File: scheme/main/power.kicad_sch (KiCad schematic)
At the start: 3 parts, among them U15 SCWN06B-15, U16 K7809-1000R3, U17 K7803-1000R3

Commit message: power scheme
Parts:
- added C61, C63: 22uF, Capacitor_SMD:C_Elec_4x5.8, symbol Device:C_Polarized
- added C62, C64, C66, C68, C70, C72, C76, C78, C80, C82: 220nF, Capacitor_SMD:C_0805_2012Metric, symbol Device:C
- added C65, C67, C69, C71, C75, C77, C81: 47uF, Capacitor_SMD:C_Elec_5x5.8, symbol Device:C_Polarized
- added C73, C74: 33nF, Capacitor_SMD:C_0805_2012Metric, symbol Device:C
- added C79: 4.7uF, Capacitor_SMD:C_0805_2012Metric, symbol Device:C
- added L1: 160uH, Inductor_SMD:L_0805_2012Metric, symbol Device:L
- added NT1: NetTie_2, symbol Device:NetTie_2
- added U18: LD1117S50TR_SOT223, Package_TO_SOT_SMD:SOT-223-3_TabPin2, symbol Regulator_Linear:LD1117S50TR_SOT223
- added U19: IFX1117MEV33HTMA1, Package_TO_SOT_SMD:SOT-223-3_TabPin2, symbol Regulator_Linear:LD1117S33TR_SOT223
- added U20: K7805-1000R3, Converter_DCDC:Converter_DCDC_RECOM_R-78HB-0.5_THT, symbol main:K7805-1000R3
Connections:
- net +24V: now also U16.1 (IN), U17.1 (IN), C69.1, C70.1, C71.1, C72.1, C74.1, L1.1
- net GND: now also U15.2 (-Vin), U15.3 (-Vin), U16.2 (GND), U17.2 (GND), C65.2, C66.2, C67.2, C68.2, C69.2, C70.2, C71.2, C72.2, C73.2, C74.2, C75.2, C76.2, NT1.1
- net +9V: now reaches U16.3 (OUT)
- net +9V: now also C65.1, C66.1, U18.3 (VI), U19.3 (VI)
- net +15V: now reaches U15.14 (+Vout)
- net +15V: now also C77.1, C78.1, C79.1, C80.1, U20.1 (IN)
- net GNDPWR: now reaches U15.16 (-Vout)
- net GNDPWR: now also C77.2, C78.2, C79.2, C80.2, C81.2, C82.2, U20.2 (GND)
- net at U15.22 (+Vin), U15.23 (+Vin): now also C73.1, C75.1, C76.1, L1.2
- net at U17.3 (OUT): now also C67.1, C68.1
- new net +3.3VA: C63.1, C64.1, U19.2 (VO)
- new net +5P: C81.1, C82.1, U20.3 (OUT)
- new net +5VA: C61.1, C62.1, U18.2 (VO)
- new net GNDA: C61.2, C62.2, C63.2, C64.2, NT1.2, U18.1 (GND), U19.1 (GND)
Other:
- note added: "Суммарная потребляемая мощность около 10Вт. Таким образом нужен блок питания 24В с выходной мощностью не менее 10Вт."
- moved on the sheet: U15, U16, U17

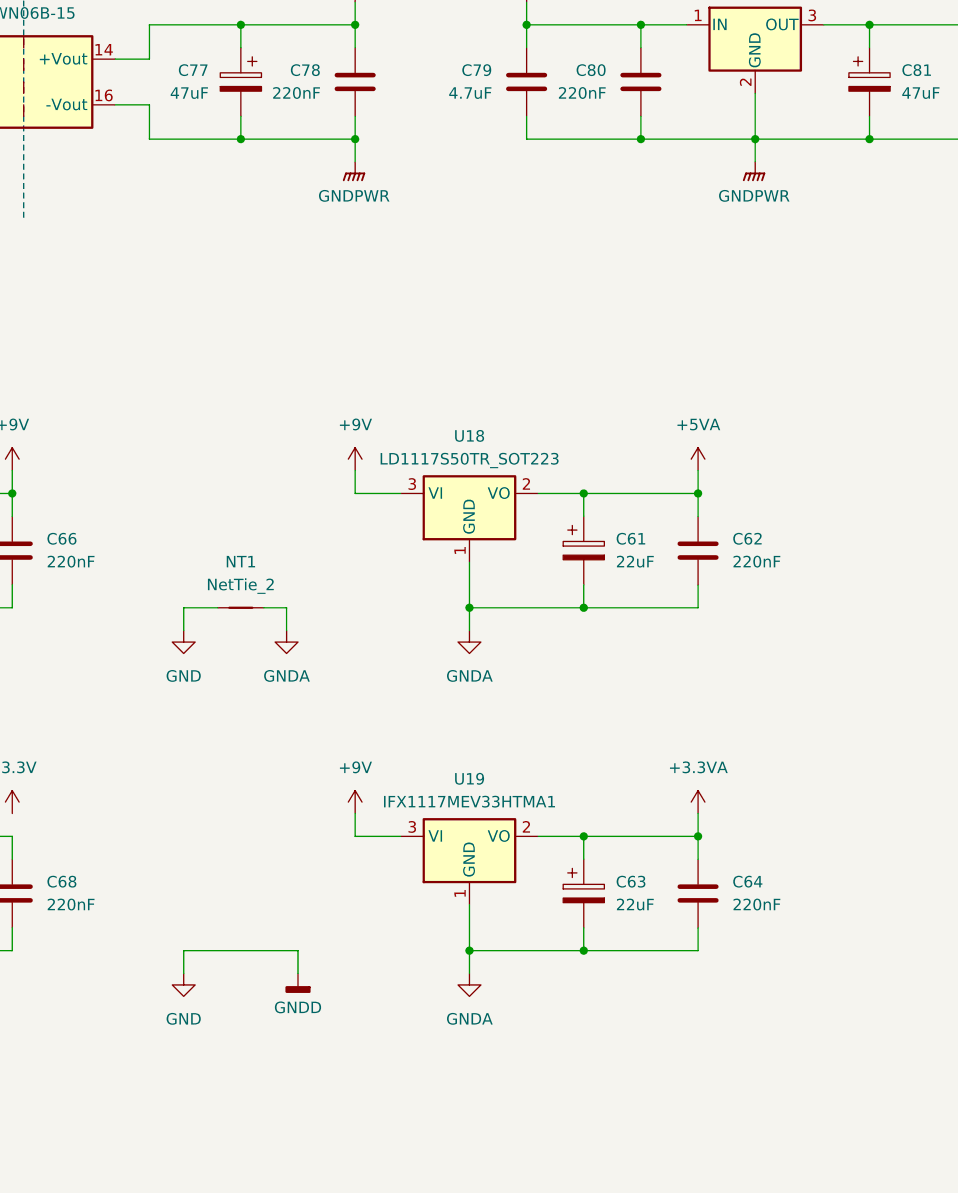
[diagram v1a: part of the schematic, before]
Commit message: separate hi power & signal gnd
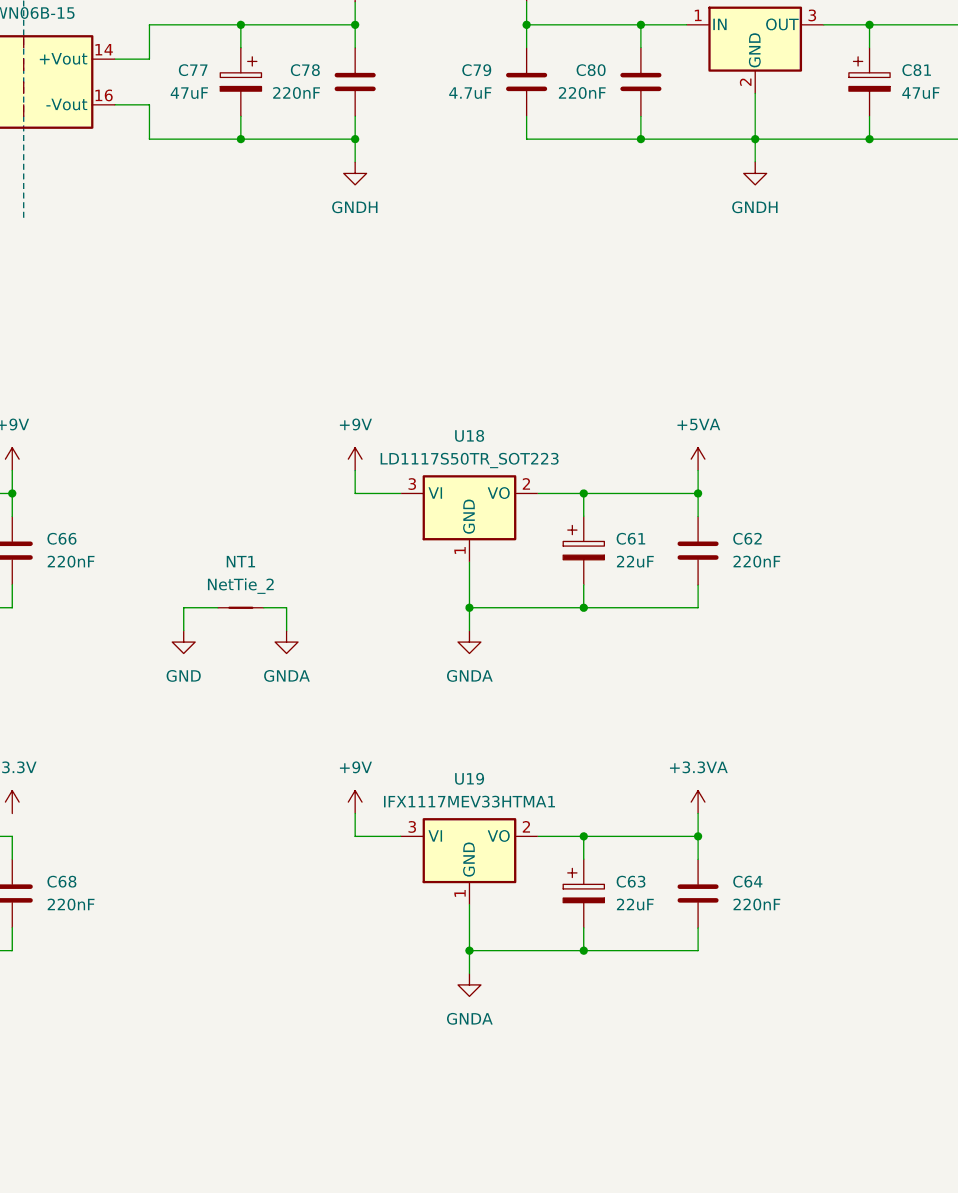
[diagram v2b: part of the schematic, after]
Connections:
- net GNDPWR renamed GNDH

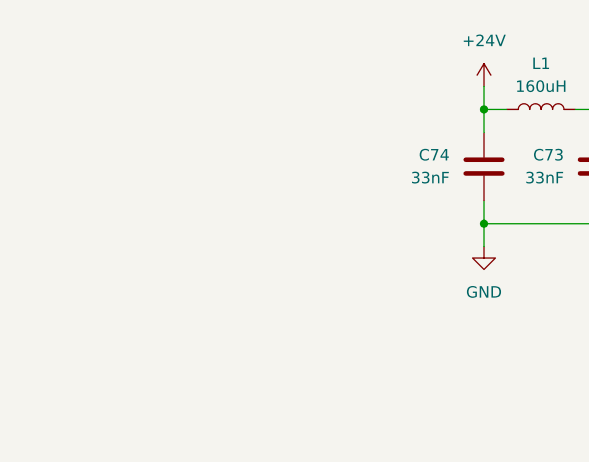
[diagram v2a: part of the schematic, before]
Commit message: added ac/dc 24V
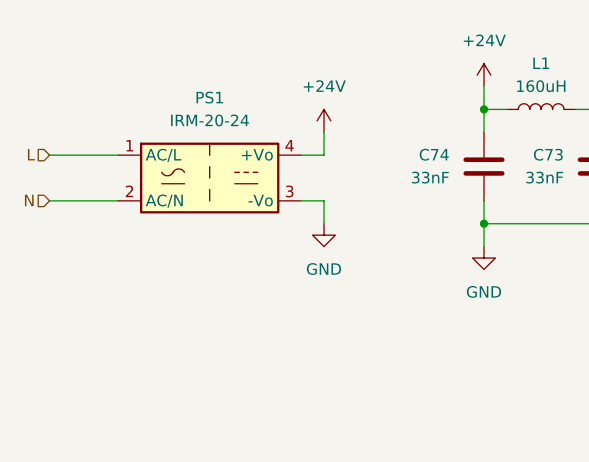
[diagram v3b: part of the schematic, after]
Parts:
- added PS1: IRM-20-24, Converter_ACDC:Converter_ACDC_MeanWell_IRM-20-xx_THT, symbol Converter_ACDC:IRM-20-24
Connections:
- net +24V: now also PS1.4 (+Vo)
- net GND: now also PS1.3 (-Vo)
- new net L: PS1.1 (AC/L)
- new net N: PS1.2 (AC/N)

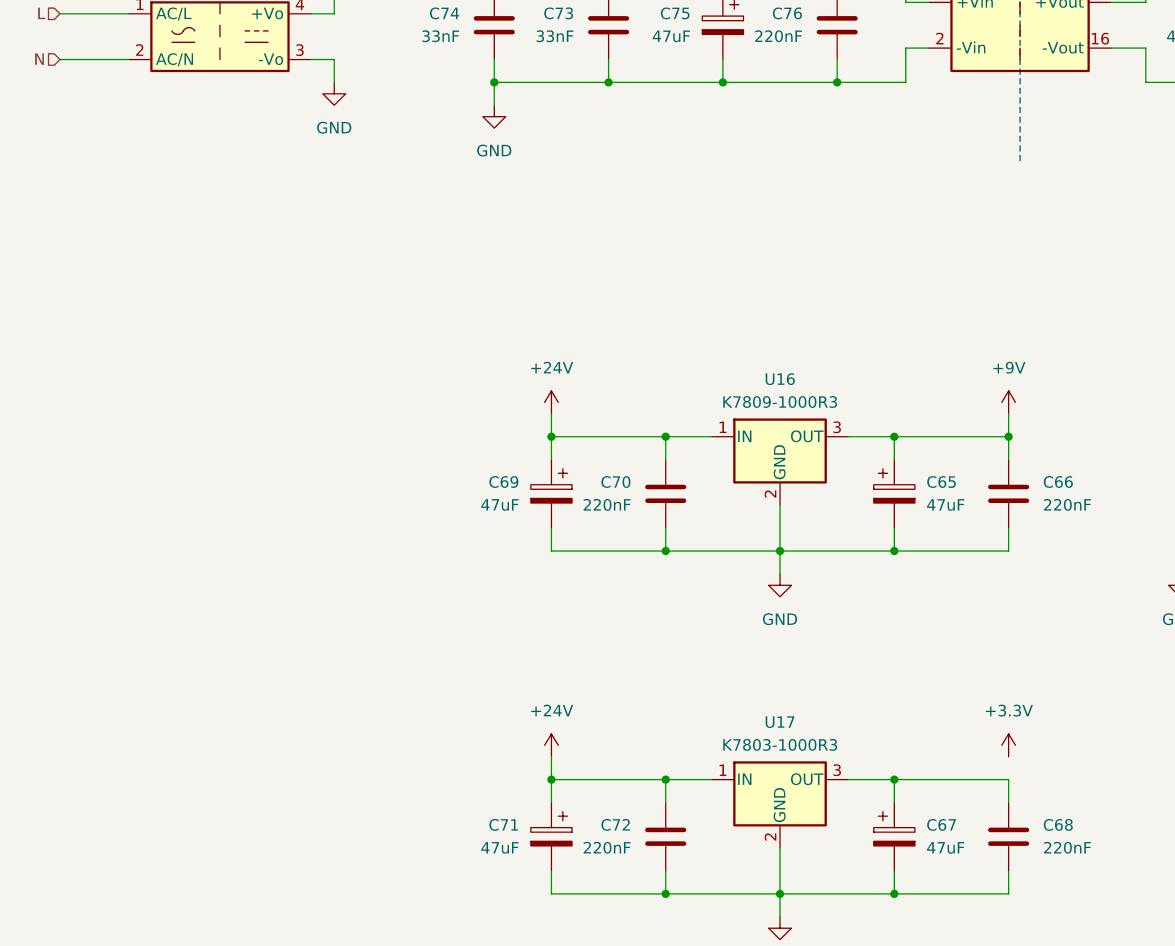
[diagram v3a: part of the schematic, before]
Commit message: digital in & out schematic
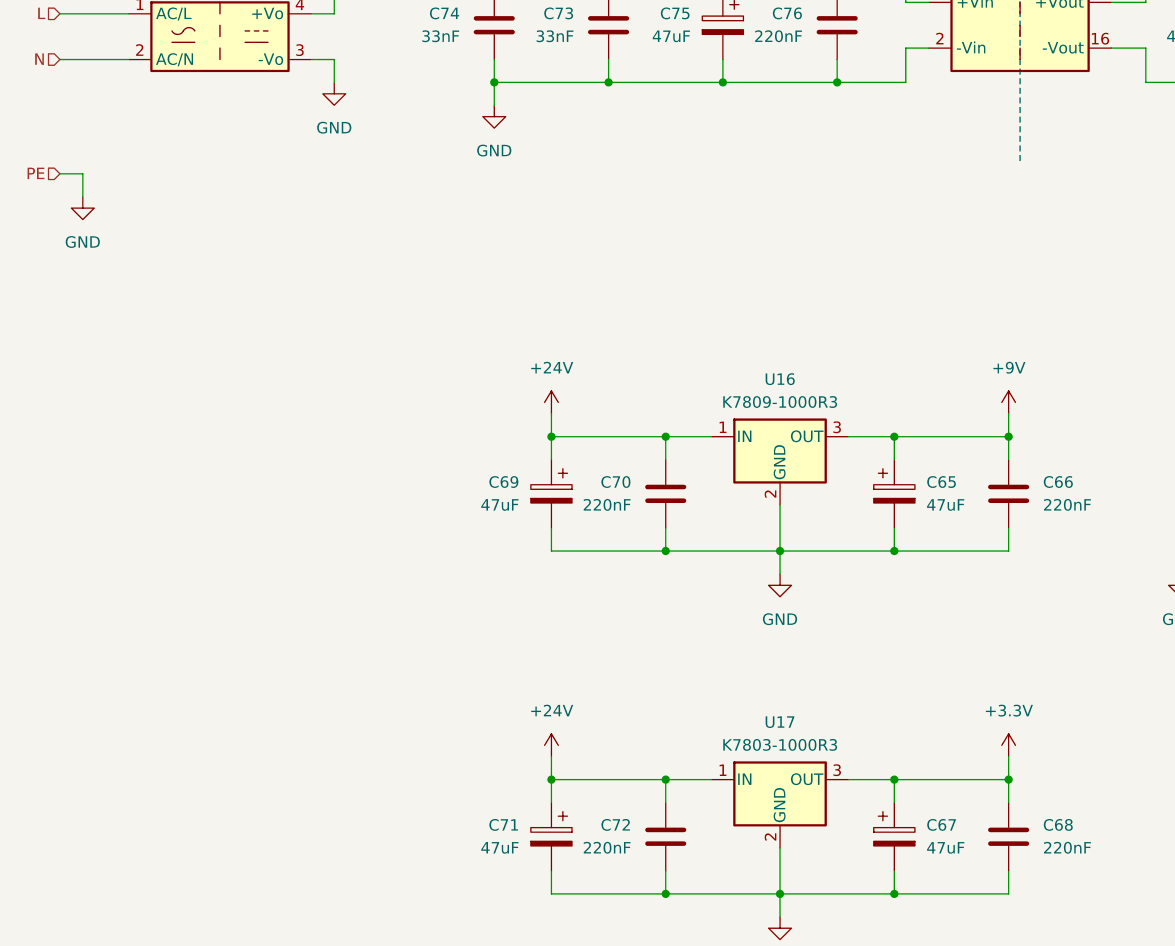
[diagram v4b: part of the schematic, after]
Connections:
- net +3.3V: now also C67.1, C68.1, U17.3 (OUT)
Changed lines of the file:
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@@
 	)
 	(junction
+		(at 132.08 118.11)
+		(diameter 0)
+		(color 0 0 0 0)
+	)
+	(junction
 		(at 157.48 40.64)
 		(diameter 0)
@@
 	(wire
 		(pts
+			(xy 132.08 115.57) (xy 132.08 118.11)
+		)
+		(stroke
+			(width 0)
+			(type default)
+		)
+	)
+	(wire
+		(pts
 			(xy 208.28 118.11) (xy 195.58 118.11)
 		)
@@
 	(wire
 		(pts
+			(xy 26.67 50.8) (xy 29.21 50.8)
+		)
+		(stroke
+			(width 0)
+			(type default)
+		)
+	)
+	(wire
+		(pts
 			(xy 81.28 90.17) (xy 81.28 92.71)
 		)
@@
 	(wire
 		(pts
+			(xy 29.21 50.8) (xy 29.21 53.34)
+		)
+		(stroke
+			(width 0)
+			(type default)
+		)
+	)
+	(wire
+		(pts
 			(xy 195.58 80.01) (xy 195.58 82.55)
 		)
@@
 		)
 	)
+	(hierarchical_label "PE"
+		(shape input)
+		(at 26.67 50.8 180)
+		(fields_autoplaced yes)
+		(effects
+			(font
+				(size 1.27 1.27)
+			)
+			(justify right)
+		)
+	)
 	(symbol
 		(lib_id "Device:C_Polarized")
@@
 					(unit 1)
 				)
+			)
+		)
+	)
+	(symbol
+		(lib_id "power:GND")
+		(at 29.21 53.34 0)
+		(unit 1)
+		(exclude_from_sim no)
+		(in_bom yes)
+		(on_board yes)
+		(dnp no)
+		(fields_autoplaced yes)
+		(property "Reference" "#PWR092"
+			(at 29.21 59.69 0)
+			(effects
+				(font
+					(size 1.27 1.27)
+				)
+				(hide yes)
+			)
+		)
+		(property "Value" "GND"
+			(at 29.21 58.42 0)
+			(effects
+				(font
+					(size 1.27 1.27)
+				)
+			)
+		)
+		(property "Footprint" ""
+			(at 29.21 53.34 0)
+			(effects
+				(font
+					(size 1.27 1.27)
+				)
+				(hide yes)
+			)
+		)
+		(property "Datasheet" ""
+			(at 29.21 53.34 0)
+			(effects
+				(font
+					(size 1.27 1.27)
+				)
+				(hide yes)
+			)
+		)
+		(property "Description" "Power symbol creates a global label with name \"GND\" , ground"
+			(at 29.21 53.34 0)
+			(effects
+				(font
+					(size 1.27 1.27)
+				)
+				(hide yes)
+			)
+		)
+		(pin "1"
+		)
+		(instances
+			(project "main"
+				(path "/c11d1dbc-4db9-4712-8d1d-5f6f7086cded/f37982a3-337b-429f-abb6-a84102507a70"
+					(reference "#PWR092")
+					(unit 1)
+				)

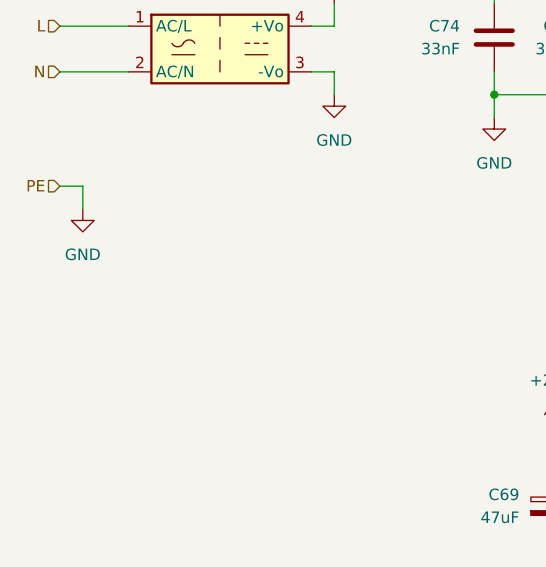
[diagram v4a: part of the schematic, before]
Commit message: toplevel layout, can bus
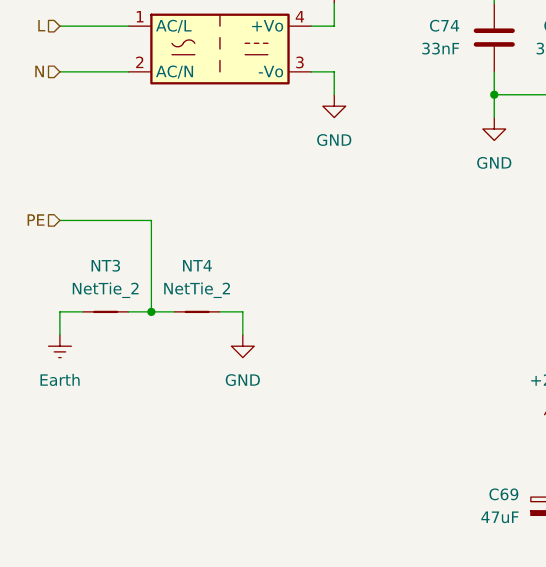
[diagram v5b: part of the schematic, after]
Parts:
- added NT3, NT4: NetTie_2, symbol Device:NetTie_2
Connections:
- net GND: now also NT4.2
- new net Earth: NT3.1
- new net PE: NT3.2, NT4.1
